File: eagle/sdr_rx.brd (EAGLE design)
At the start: 88.9 x 41.3 mm, 73 parts

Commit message: update eagle files
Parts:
- added C13: 82p, BeagleBone_Black_Wireless:R0805
- added E$40, E$42, E$43, E$44, E$45, E$46, E$47, E$48, E$49, E$50, E$51, E$52: (no value), BeagleBone_Black_Wireless:R0402
- added E$41: (no value), SparkFun-Clocks:OSCILLATOR-SMD-7.5X5.2-6PIN
- moved C12 7.62 mm to (50.8, 4.45)
- moved L14 7.62 mm to (50.2, 1.91)
- turned E$5 to 90 degrees
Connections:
- new net S$35: E$41.3, E$43.1, E$45.2
- new net S$36: E$41.NC1, E$42.1, E$44.1
- new net S$37: E$3.10, E$40.1, E$42.2
- new net S$38: E$3.11, E$40.2, E$43.2
- new net S$39: E$41.1, E$47.1, E$48.1
- new net S$41: E$3.6, E$49.2, E$50.1
- new net S$42: E$5.14, E$5.18, E$5.42, E$5.47, E$5.58, E$5.68, E$5.74, E$5.8, E$5.80, E$5.87, E$5.91, E$5.95
- net GND: now also C13.2, E$3.28, E$3.29, E$41.2, E$41.NC0, E$44.2, E$45.1, E$46.2, E$47.2, E$50.2, E$51.2, E$52.2
- net V1.1: now also E$5.17, E$5.38, E$5.66, E$5.81
- net V1.8: now also E$3.2, E$3.35, E$5.11, E$5.26, E$5.45, E$5.67, E$5.79, E$5.96, E$51.1, E$52.1
- net V1.8A: now also E$3.27, E$3.30, E$3.7, E$49.1
- net V3.3: now also C13.1, E$41.4, E$46.1
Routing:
- net V3.3: track 38.1 -> 53.1 mm, vias 0 -> 1
- net GND: track 22.3 -> 32.8 mm, vias 246 -> 260
- net V1.8: track 13.2 -> 21.9 mm
- net V3.3A: track 32.3 -> 24.7 mm
- net S$36: track 0.00 -> 5.92 mm
- net S$35: track 0.00 -> 5.92 mm
- net V1.8A: track 35.7 -> 41.0 mm
- net S$39: track 0.00 -> 4.12 mm
- net S$38: track 0.00 -> 3.47 mm
- net S$37: track 0.00 -> 3.26 mm
- net S$41: track 0.00 -> 3.11 mm

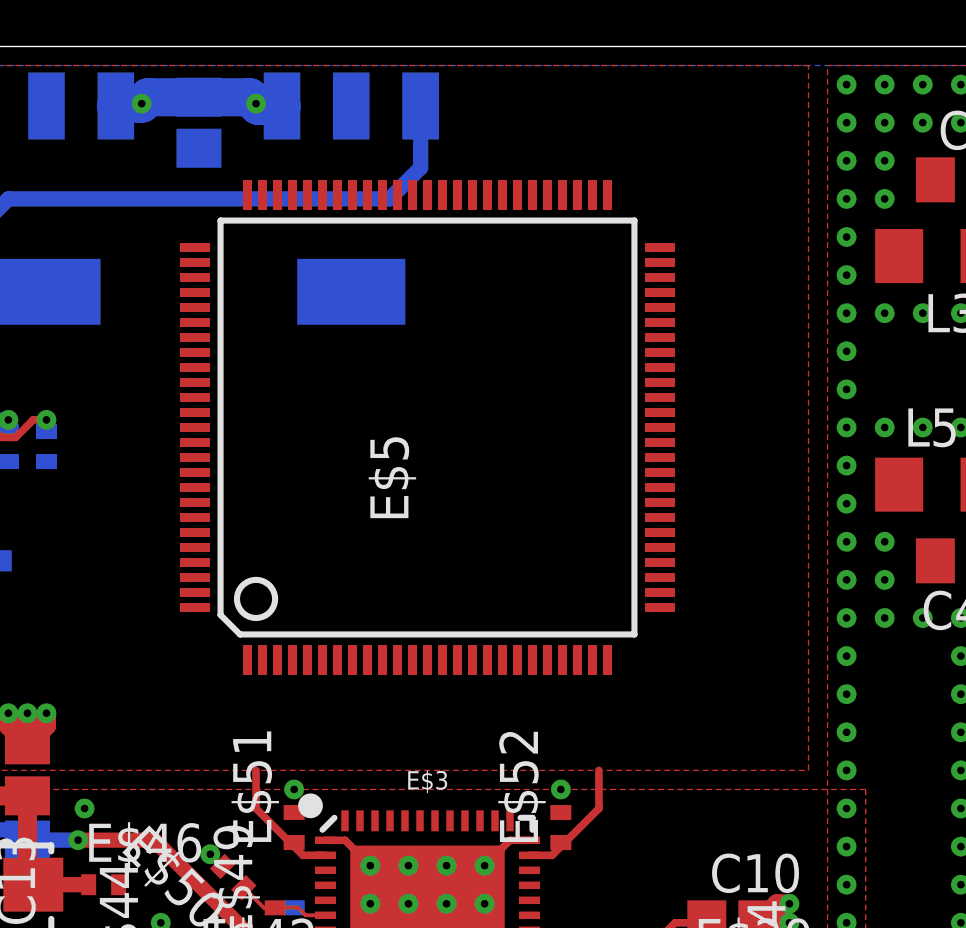
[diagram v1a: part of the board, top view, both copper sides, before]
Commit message: add down-converter board layout
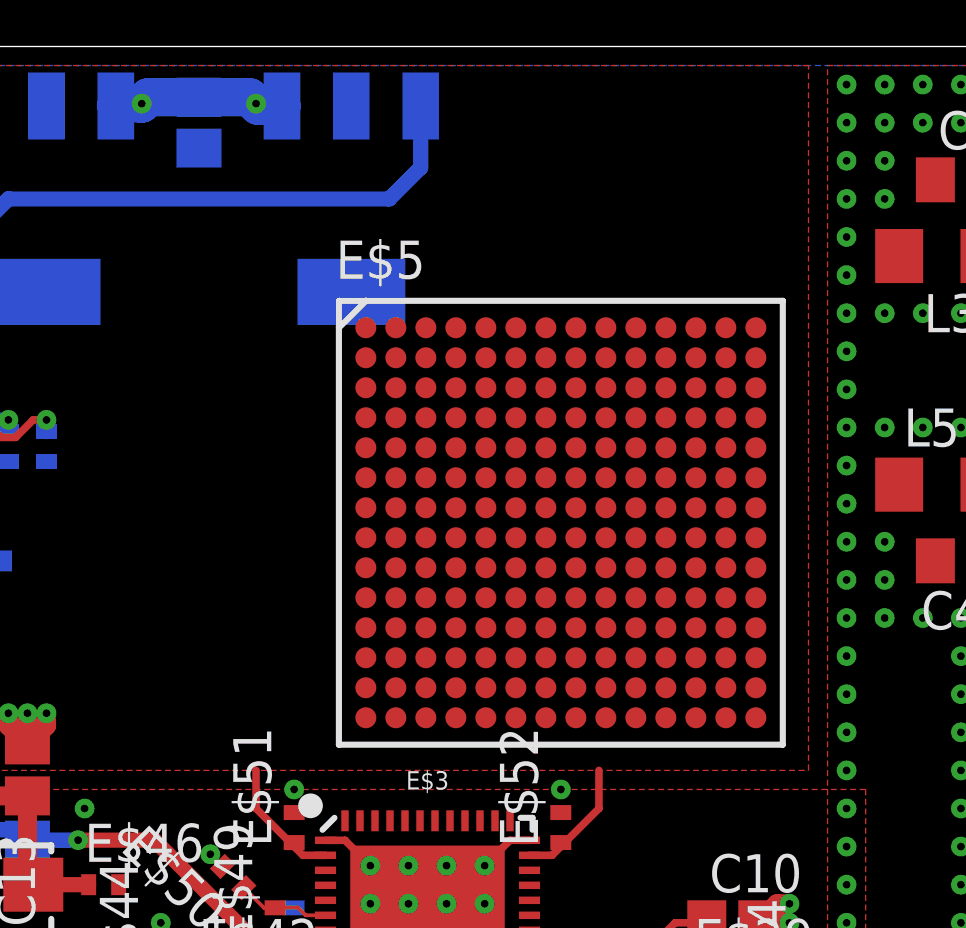
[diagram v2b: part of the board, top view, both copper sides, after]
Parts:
- E$5: device xilinx-xcv:VQ100 -> micro-intel:PBGA196
- moved E$5 5.46 mm to (59.7, 25.4), turned to 0 degrees
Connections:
- removed net S$42: E$5.14, E$5.18, E$5.42, E$5.47, E$5.58, E$5.68, E$5.74, E$5.8, E$5.80, E$5.87, E$5.91, E$5.95
- net V1.1: no longer E$5.17, E$5.38, E$5.66, E$5.81
- net V1.8: no longer E$5.11, E$5.26, E$5.45, E$5.67, E$5.79, E$5.96
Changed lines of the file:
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@@
 <attribute name="VALUE" x="59.563" y="6.35" size="1.27" layer="27" rot="R270"/>
-</element>
-<element name="E$5" library="xilinx-xcv" library_urn="urn:adsk.eagle:library:417" package="VQ100" value="" x="55.245" y="28.575" smashed="yes" rot="R90">
-<attribute name="NAME" x="54.61" y="25.4" size="1.27" layer="25" rot="R90"/>
-<attribute name="VALUE" x="57.15" y="25.4" size="1.27" layer="27" rot="R90"/>
 </element>
 <element name="E$6" library="transistor" library_urn="urn:adsk.eagle:library:402" package="SOT223" value="" x="33.02" y="20.955" smashed="yes" rot="MR90">
@@
 <attribute name="NAME" x="58.928" y="14.605" size="1.27" layer="25" rot="R90"/>
 <attribute name="VALUE" x="61.722" y="14.605" size="1.27" layer="27" rot="R90"/>
+</element>
+<element name="E$5" library="micro-intel" library_urn="urn:adsk.eagle:library:287" package="PBGA196" value="" x="59.69" y="25.4" smashed="yes">
+<attribute name="NAME" x="52.19" y="33.535" size="1.27" layer="25"/>
+<attribute name="VALUE" x="52.19" y="15.995" size="1.27" layer="27"/>
 </element>
 </elements>
@@
 <wire x1="55.0164" y1="39.2938" x2="55.0164" y2="37.2364" width="0.508" layer="16"/>
 <wire x1="55.0164" y1="37.2364" x2="53.975" y2="36.195" width="0.508" layer="16"/>
-<contactref element="E$5" pad="17"/>
-<contactref element="E$5" pad="38"/>
-<contactref element="E$5" pad="81"/>
-<contactref element="E$5" pad="66"/>
-<wire x1="57.245" y1="20.825" x2="62.995" y2="28.575" width="0" layer="19" extent="1-1"/>
-<wire x1="53.745" y1="36.325" x2="62.995" y2="28.575" width="0" layer="19" extent="1-1"/>
-<wire x1="55.0164" y1="39.2938" x2="53.745" y2="36.325" width="0" layer="19" extent="1-16"/>
-<wire x1="47.495" y1="32.075" x2="41.275" y2="28.829" width="0" layer="19" extent="1-1"/>
 </signal>
 <signal name="S$13">
@@
 <wire x1="50.8" y1="14.74" x2="50.8" y2="14.605" width="0.254" layer="1"/>
 <wire x1="59.69" y1="14.74" x2="59.69" y2="14.605" width="0.254" layer="1"/>
-<contactref element="E$5" pad="45"/>
-<contactref element="E$5" pad="26"/>
-<contactref element="E$5" pad="67"/>
-<contactref element="E$5" pad="79"/>
-<contactref element="E$5" pad="96"/>
-<contactref element="E$5" pad="11"/>
-<wire x1="62.995" y1="22.575" x2="62.995" y2="32.075" width="0" layer="19" extent="1-1"/>
-<wire x1="53.245" y1="36.325" x2="50.3936" y2="39.2938" width="0" layer="19" extent="1-16"/>
-<wire x1="54.245" y1="20.825" x2="49.53" y2="17.145" width="0" layer="19" extent="1-1"/>
-<wire x1="47.495" y1="24.575" x2="42.545" y2="28.44" width="0" layer="19" extent="1-16"/>
-<wire x1="47.495" y1="33.075" x2="42.545" y2="28.829" width="0" layer="19" extent="1-1"/>
+<wire x1="37.084" y1="34.29" x2="44.8564" y2="39.2938" width="0" layer="19" extent="16-16"/>
+<wire x1="40.23" y1="28.325" x2="37.58" y2="31.975" width="0" layer="19" extent="1-1"/>
+<wire x1="37.08" y1="25.175" x2="40.23" y2="28.325" width="0" layer="19" extent="1-1"/>
+<wire x1="49.53" y1="17.145" x2="42.545" y2="28.44" width="0" layer="19" extent="1-16"/>
+<wire x1="58.645" y1="14.315" x2="51.845" y2="14.315" width="0" layer="19" extent="1-1"/>
 </signal>
 <signal name="S$12">
@@
 <wire x1="49.791996875" y1="12.565" x2="49.121553125" y2="13.23544375" width="0.127" layer="1"/>
 </signal>
-<signal name="S$42">
-<contactref element="E$5" pad="47"/>
-<contactref element="E$5" pad="42"/>
-<contactref element="E$5" pad="58"/>
-<contactref element="E$5" pad="68"/>
-<contactref element="E$5" pad="74"/>
-<contactref element="E$5" pad="80"/>
-<contactref element="E$5" pad="87"/>
-<contactref element="E$5" pad="91"/>
-<contactref element="E$5" pad="95"/>
-<contactref element="E$5" pad="8"/>
-<contactref element="E$5" pad="14"/>
-<contactref element="E$5" pad="18"/>
-<wire x1="62.995" y1="30.575" x2="62.995" y2="33.075" width="0" layer="19" extent="1-1"/>
-<wire x1="57.745" y1="36.325" x2="62.995" y2="33.075" width="0" layer="19" extent="1-1"/>
-<wire x1="52.745" y1="36.325" x2="57.745" y2="36.325" width="0" layer="19" extent="1-1"/>
-<wire x1="49.745" y1="36.325" x2="52.745" y2="36.325" width="0" layer="19" extent="1-1"/>
-<wire x1="47.495" y1="32.575" x2="49.745" y2="36.325" width="0" layer="19" extent="1-1"/>
-<wire x1="47.495" y1="29.075" x2="47.495" y2="32.575" width="0" layer="19" extent="1-1"/>
-<wire x1="47.495" y1="27.075" x2="47.495" y2="29.075" width="0" layer="19" extent="1-1"/>
-<wire x1="47.495" y1="25.075" x2="47.495" y2="27.075" width="0" layer="19" extent="1-1"/>
-<wire x1="52.745" y1="20.825" x2="47.495" y2="25.075" width="0" layer="19" extent="1-1"/>
-<wire x1="55.745" y1="20.825" x2="52.745" y2="20.825" width="0" layer="19" extent="1-1"/>
-<wire x1="57.745" y1="20.825" x2="55.745" y2="20.825" width="0" layer="19" extent="1-1"/>
-</signal>
 </signals>
